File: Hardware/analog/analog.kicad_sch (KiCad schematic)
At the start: 0 parts

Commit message: Analog board tweaks
- Moved a few traces and components around to accomodate other changes
  in the controller stuff, preparation for some sort of cleanup

- Aesthetic moves of labels on controller board
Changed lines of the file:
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@@
     (stroke (width 0) (type default))
   )
-  (label "ISense_{0" (at 219.075 35.56 0) (fields_autoplaced)
+  (label "ISense_{0}" (at 219.075 35.56 0) (fields_autoplaced)
     (effects (font (size 1.27 1.27)) (justify left bottom))
   )
@@
     (effects (font (size 1.27 1.27)) (justify left bottom))
   )
-  (label "ISet_{0" (at 161.925 78.74 0) (fields_autoplaced)
-    (effects (font (size 1.27 1.27)) (justify left bottom))
-  )
-  (label "ISense_{1" (at 161.925 90.17 0) (fields_autoplaced)
-    (effects (font (size 1.27 1.27)) (justify left bottom))
-  )
-  (label "ISense_{1" (at 219.075 38.1 0) (fields_autoplaced)
+  (label "ISet_{0}" (at 161.925 78.74 0) (fields_autoplaced)
+    (effects (font (size 1.27 1.27)) (justify left bottom))
+  )
+  (label "ISense_{1}" (at 161.925 90.17 0) (fields_autoplaced)
+    (effects (font (size 1.27 1.27)) (justify left bottom))
+  )
+  (label "ISense_{1}" (at 219.075 38.1 0) (fields_autoplaced)
     (effects (font (size 1.27 1.27)) (justify left bottom))
   )
@@
     (effects (font (size 1.27 1.27)) (justify left bottom))
   )
-  (label "ISet_{1" (at 219.075 30.48 0) (fields_autoplaced)
-    (effects (font (size 1.27 1.27)) (justify left bottom))
-  )
-  (label "ISet_{1" (at 161.925 81.28 0) (fields_autoplaced)
+  (label "ISet_{1}" (at 219.075 30.48 0) (fields_autoplaced)
+    (effects (font (size 1.27 1.27)) (justify left bottom))
+  )
+  (label "ISet_{1}" (at 161.925 81.28 0) (fields_autoplaced)
     (effects (font (size 1.27 1.27)) (justify left bottom))
   )
@@
     (effects (font (size 1.27 1.27)) (justify left bottom))
   )
-  (label "ISet_{0" (at 219.075 27.94 0) (fields_autoplaced)
-    (effects (font (size 1.27 1.27)) (justify left bottom))
-  )
-  (label "ISense_{0" (at 161.925 85.09 0) (fields_autoplaced)
+  (label "ISet_{0}" (at 219.075 27.94 0) (fields_autoplaced)
+    (effects (font (size 1.27 1.27)) (justify left bottom))
+  )
+  (label "ISense_{0}" (at 161.925 85.09 0) (fields_autoplaced)
     (effects (font (size 1.27 1.27)) (justify left bottom))
   )
@@
     )
     (path "/ebb39e00-184a-4d9a-998d-a9c1346d5a30/8034a9d2-228a-47f5-9e42-60bb92940d1f"
-      (reference "R502") (unit 1) (value "10k") (footprint "Resistor_SMD:R_0805_2012Metric_Pad1.20x1.40mm_HandSolder")
+      (reference "R502") (unit 1) (value "5k6") (footprint "Resistor_SMD:R_0805_2012Metric_Pad1.20x1.40mm_HandSolder")
     )
     (path "/ebb39e00-184a-4d9a-998d-a9c1346d5a30/d4ade582-8aad-40e5-8e88-07c361125e22"

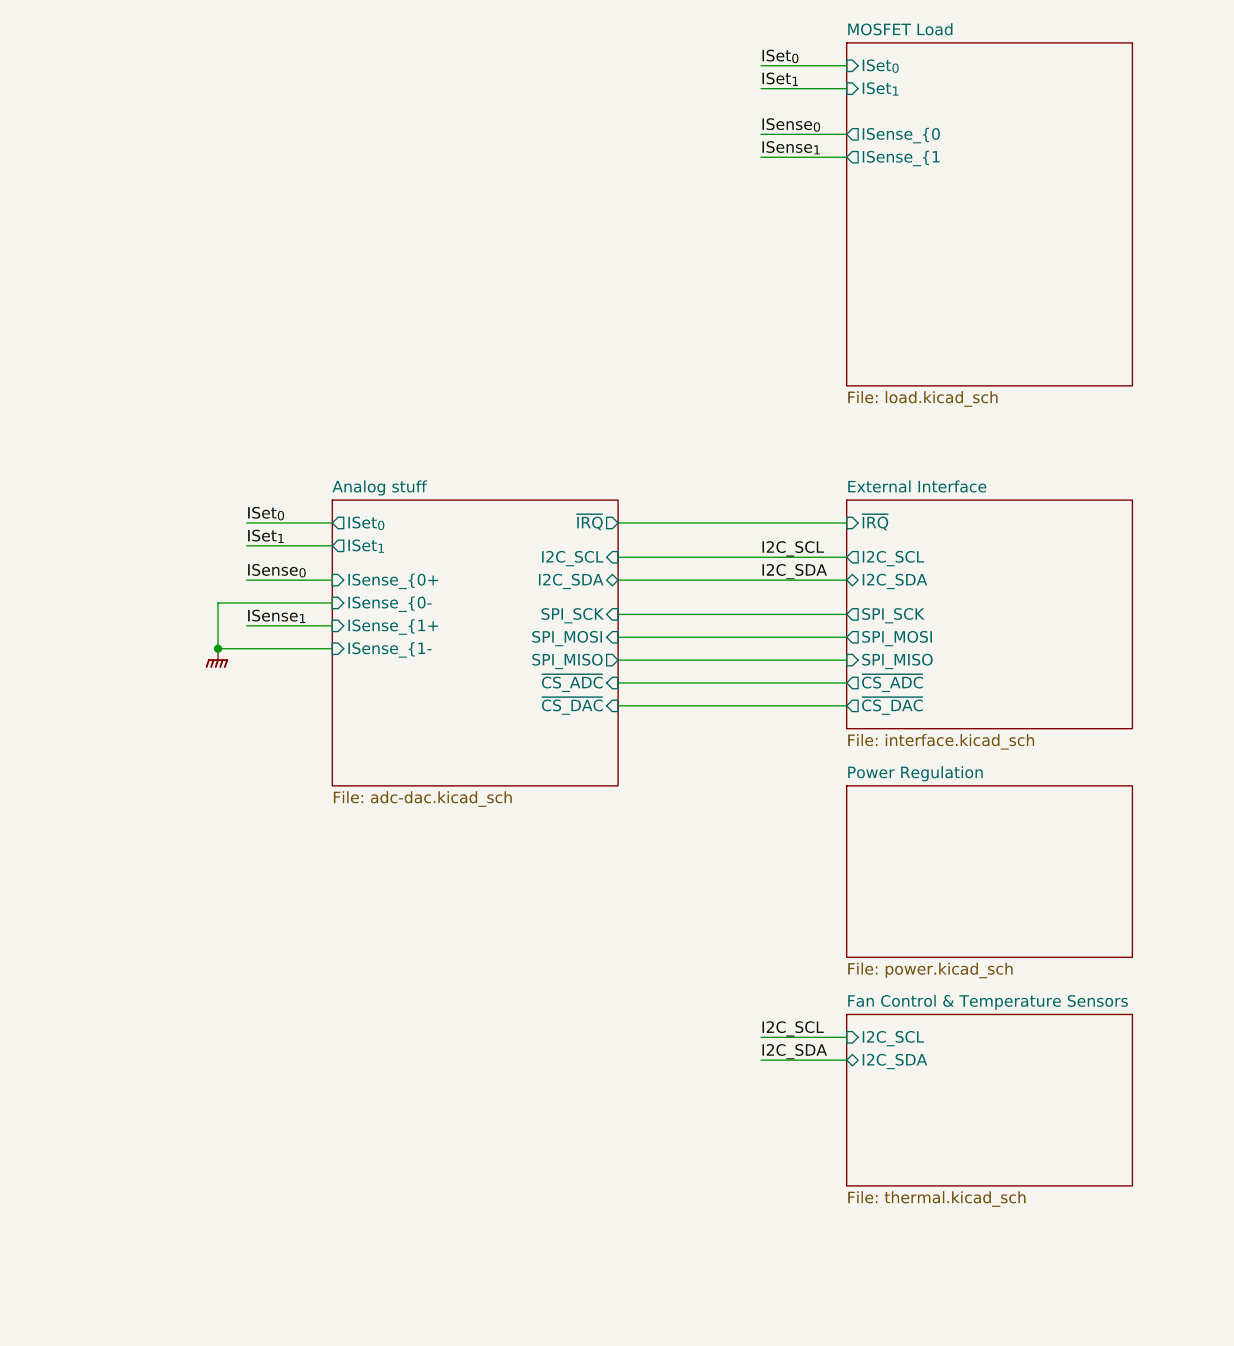
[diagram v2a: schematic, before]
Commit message: Analog board layout
- Started work on adding the voltage sense circuitry, including the
  selector relay, IO expander to drive the relay, and the second ADC to
  convert the voltage values

- Changed the layout of analog board to better take advantage of
  available space

- Minor changes to front panel layout for aesthetics
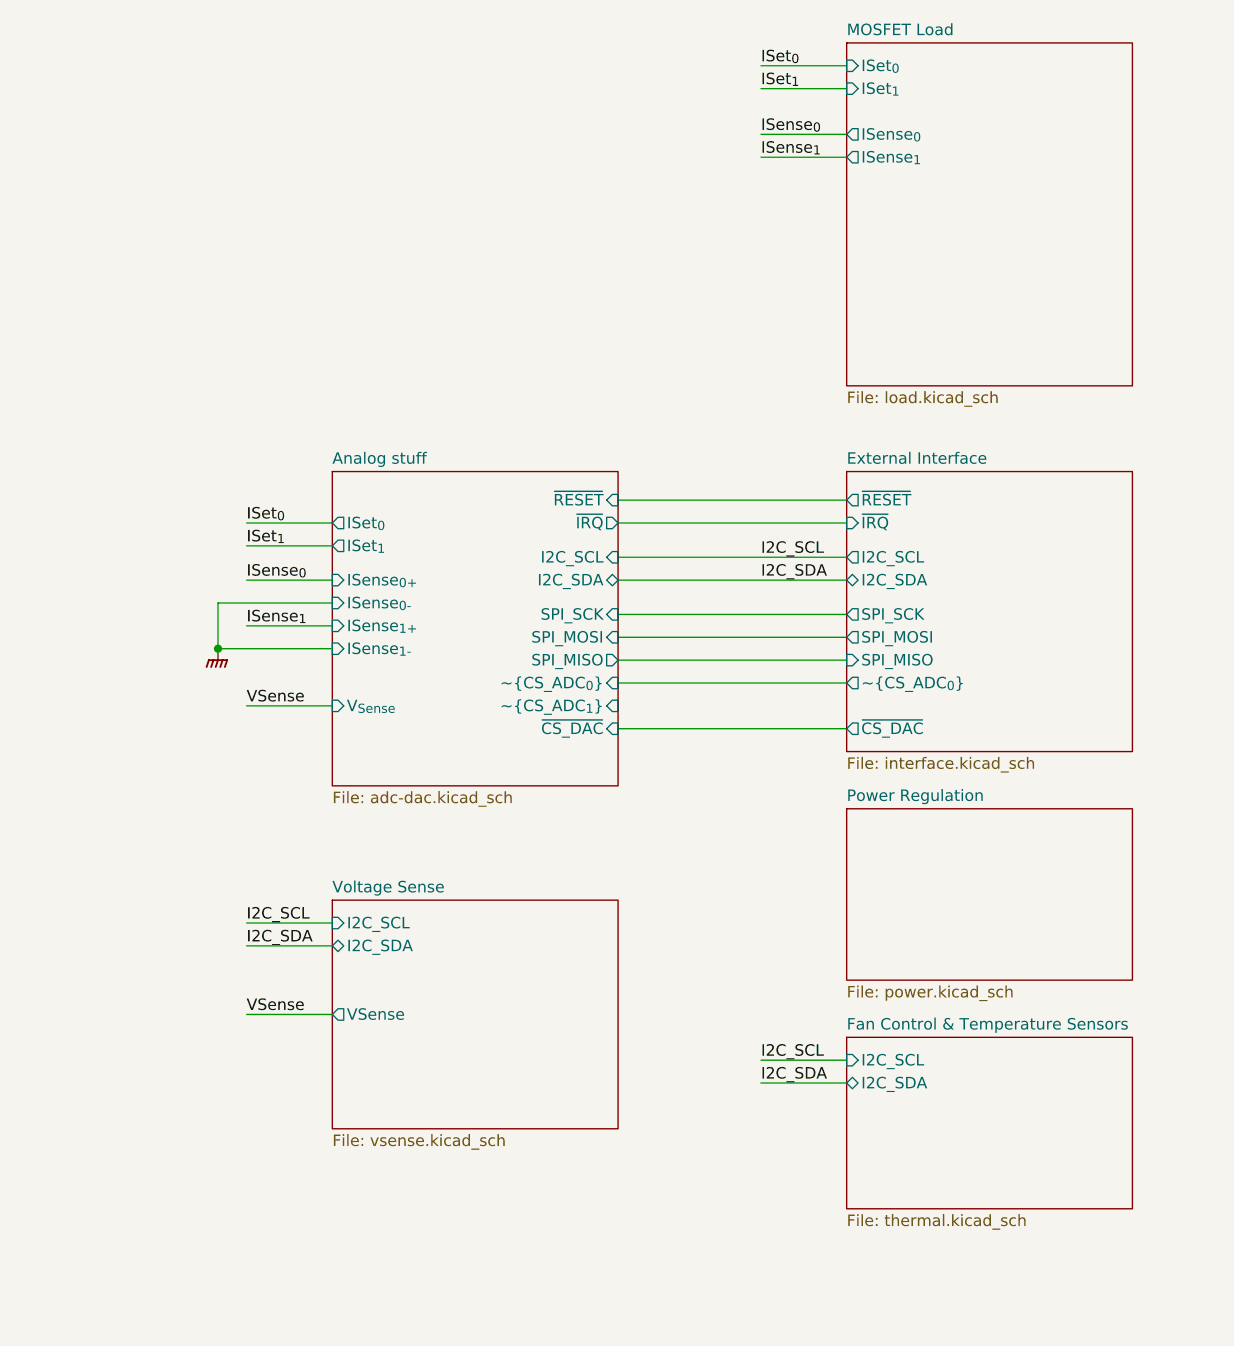
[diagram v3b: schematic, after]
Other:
- added sheet Voltage Sense (vsense.kicad_sch)
- sheet Analog stuff ports: added ISense_{0+}, ISense_{0-}, ISense_{1+}, ISense_{1-}, V_{Sense}, ~{CS_ADC_{0}}, ~{CS_ADC_{1}}, ~{RESET}; removed ISense_{0+, ISense_{0-, ISense_{1+, ISense_{1-, ~{CS_ADC}
- sheet External Interface ports: added ~{CS_ADC_{0}}, ~{RESET}; removed ~{CS_ADC}
- sheet MOSFET Load ports: added ISense_{0}, ISense_{1}; removed ISense_{0, ISense_{1

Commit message: Mostly finished up analog load board
- Finished routing most signals

- Connected relay drive to bonus I2C GPIO controller, and routed the
  rest of the voltage sense stuff

- Routed the reset signal to the DAC, so that when the board is reset,
  the current output will be reset to zero as well without processor
  intervention

- Replaced most passives with 0603/1608 size
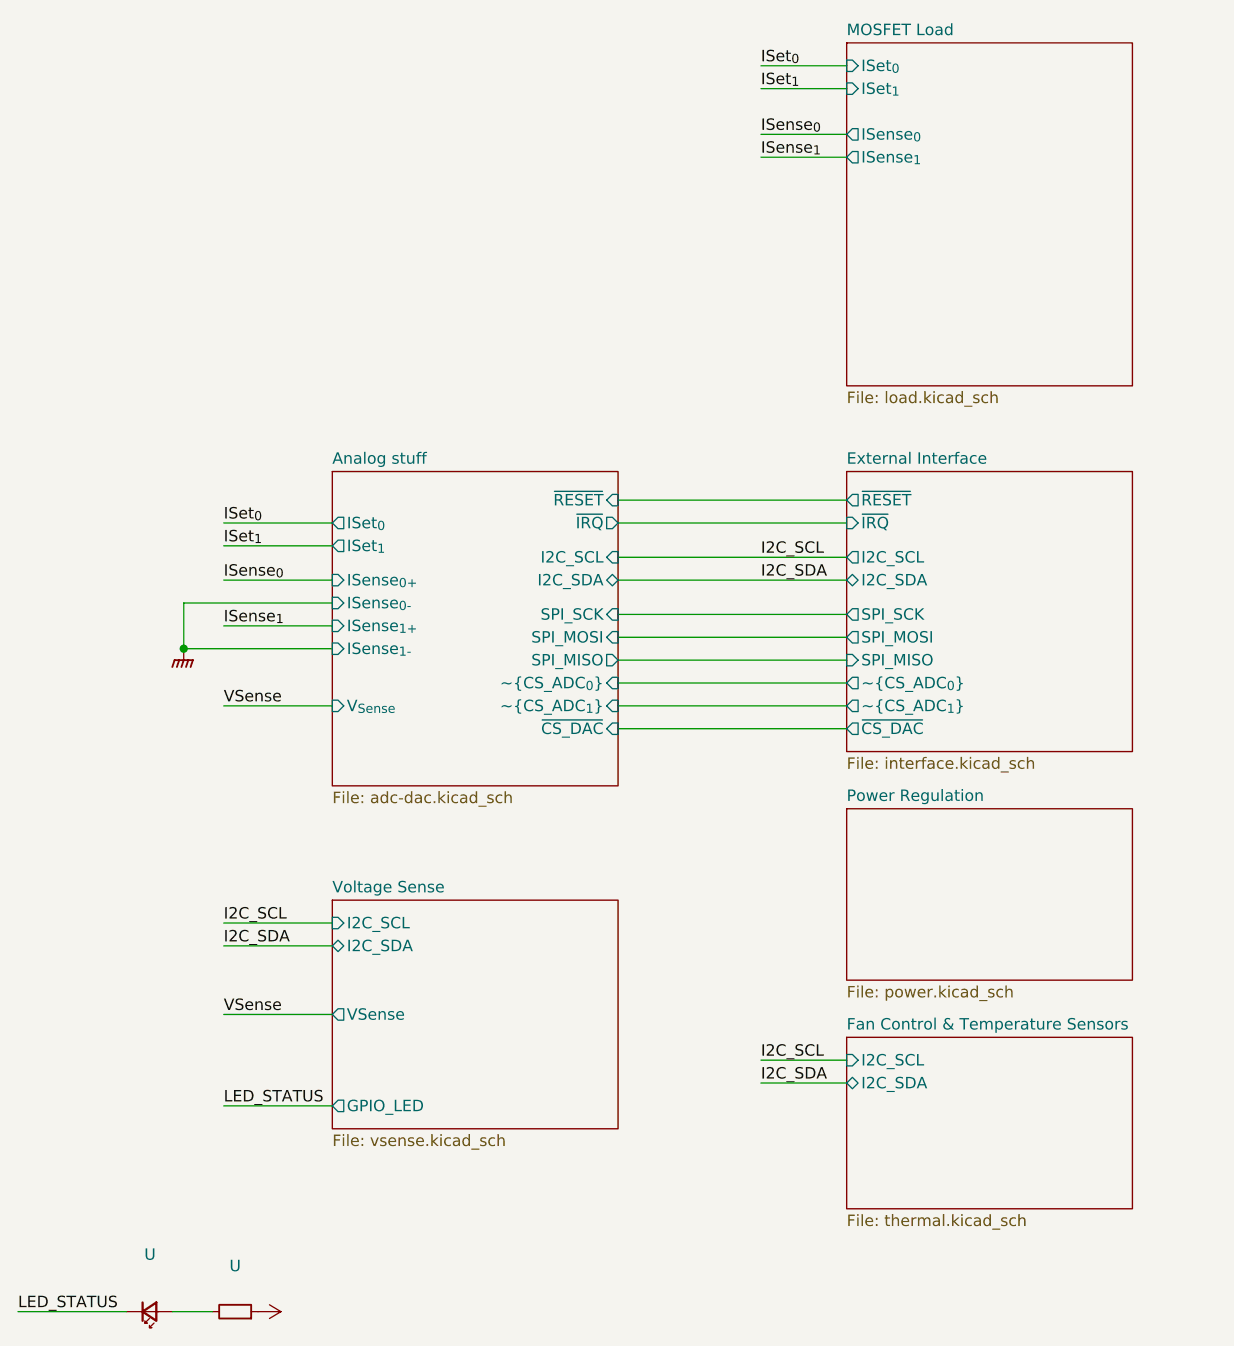
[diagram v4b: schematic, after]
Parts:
- added U: (no value), symbol Device:LED_Small
- added U: (no value), symbol Device:R_Small
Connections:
- new net: U.2, U.2 (A)
- new net +3V3: U.1
- new net LED_STATUS: U.1 (K)
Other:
- sheet External Interface ports: added ~{CS_ADC_{1}}; removed none
- sheet Voltage Sense ports: added GPIO_LED; removed none

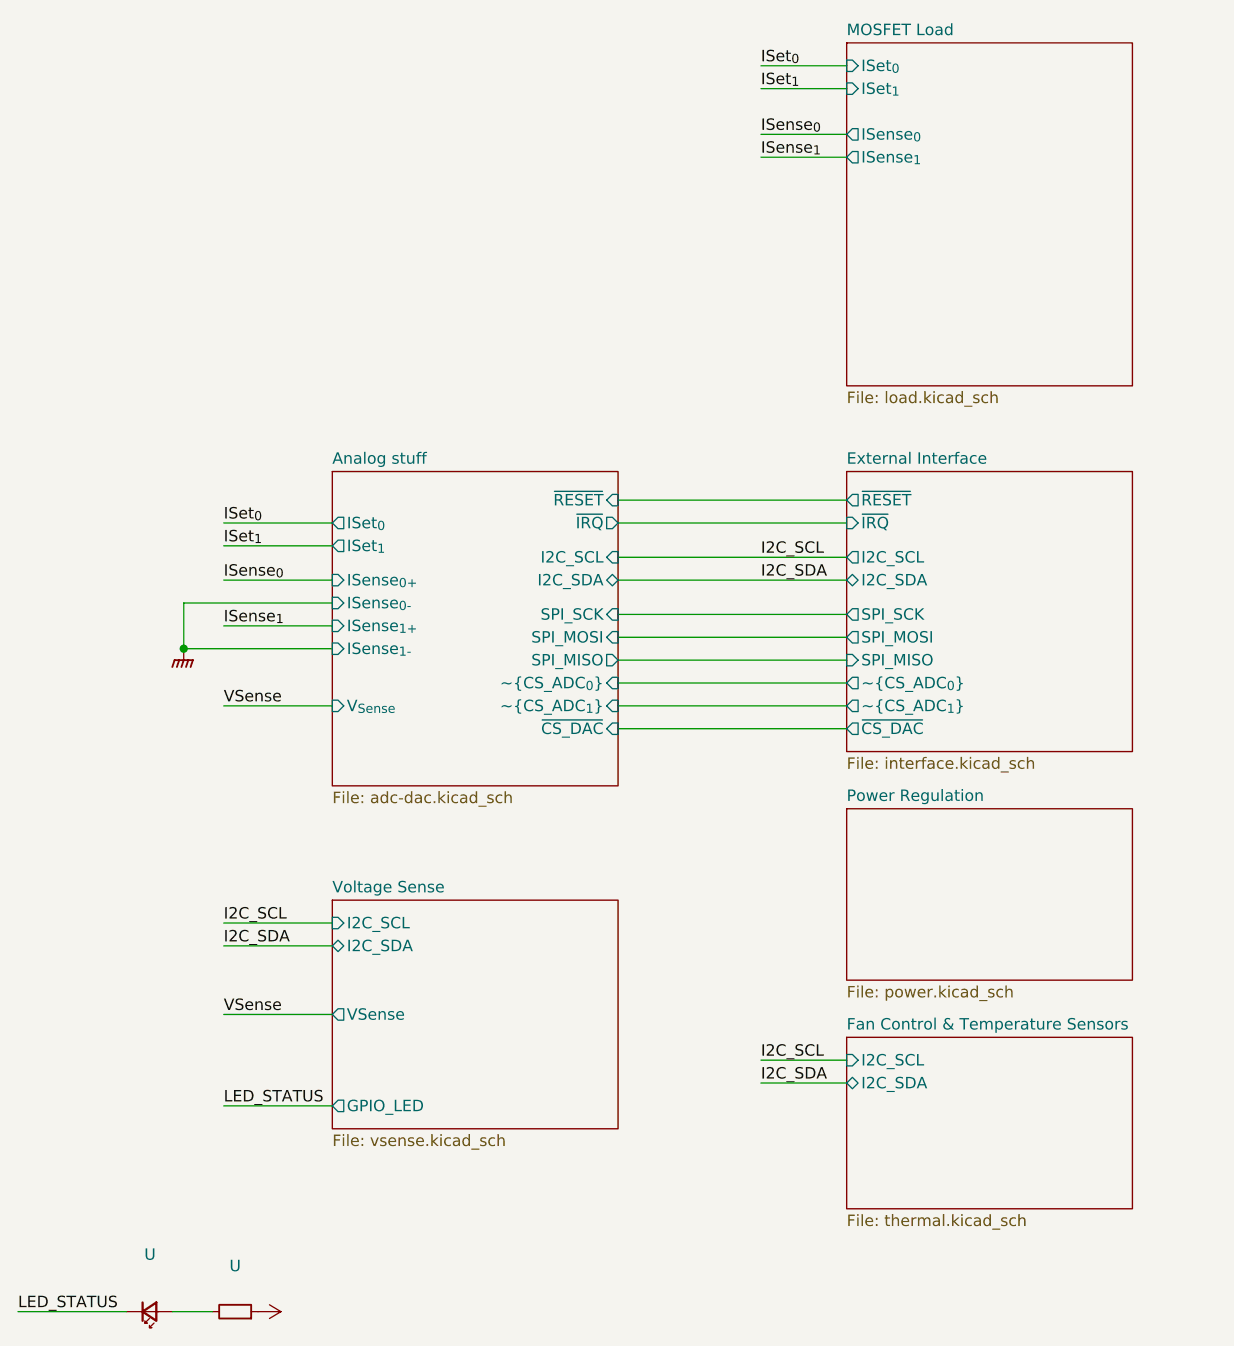
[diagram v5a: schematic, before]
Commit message: Temperature sensing & cleanup for analog board
- Added the auxiliary temperature sensing ADC, and routed it to the
  analog temperature sensors on the front and rear of the MOSFET
  heatsink

- Added an LM75 sensor to measure the analog board ambient temperature
  (for better temperature control/fan control)

  This may end up being a DNP item if it's not really useful or
  otherwise necessary.

- Fixes to a few symbols (namely pin directions) to pass ERC
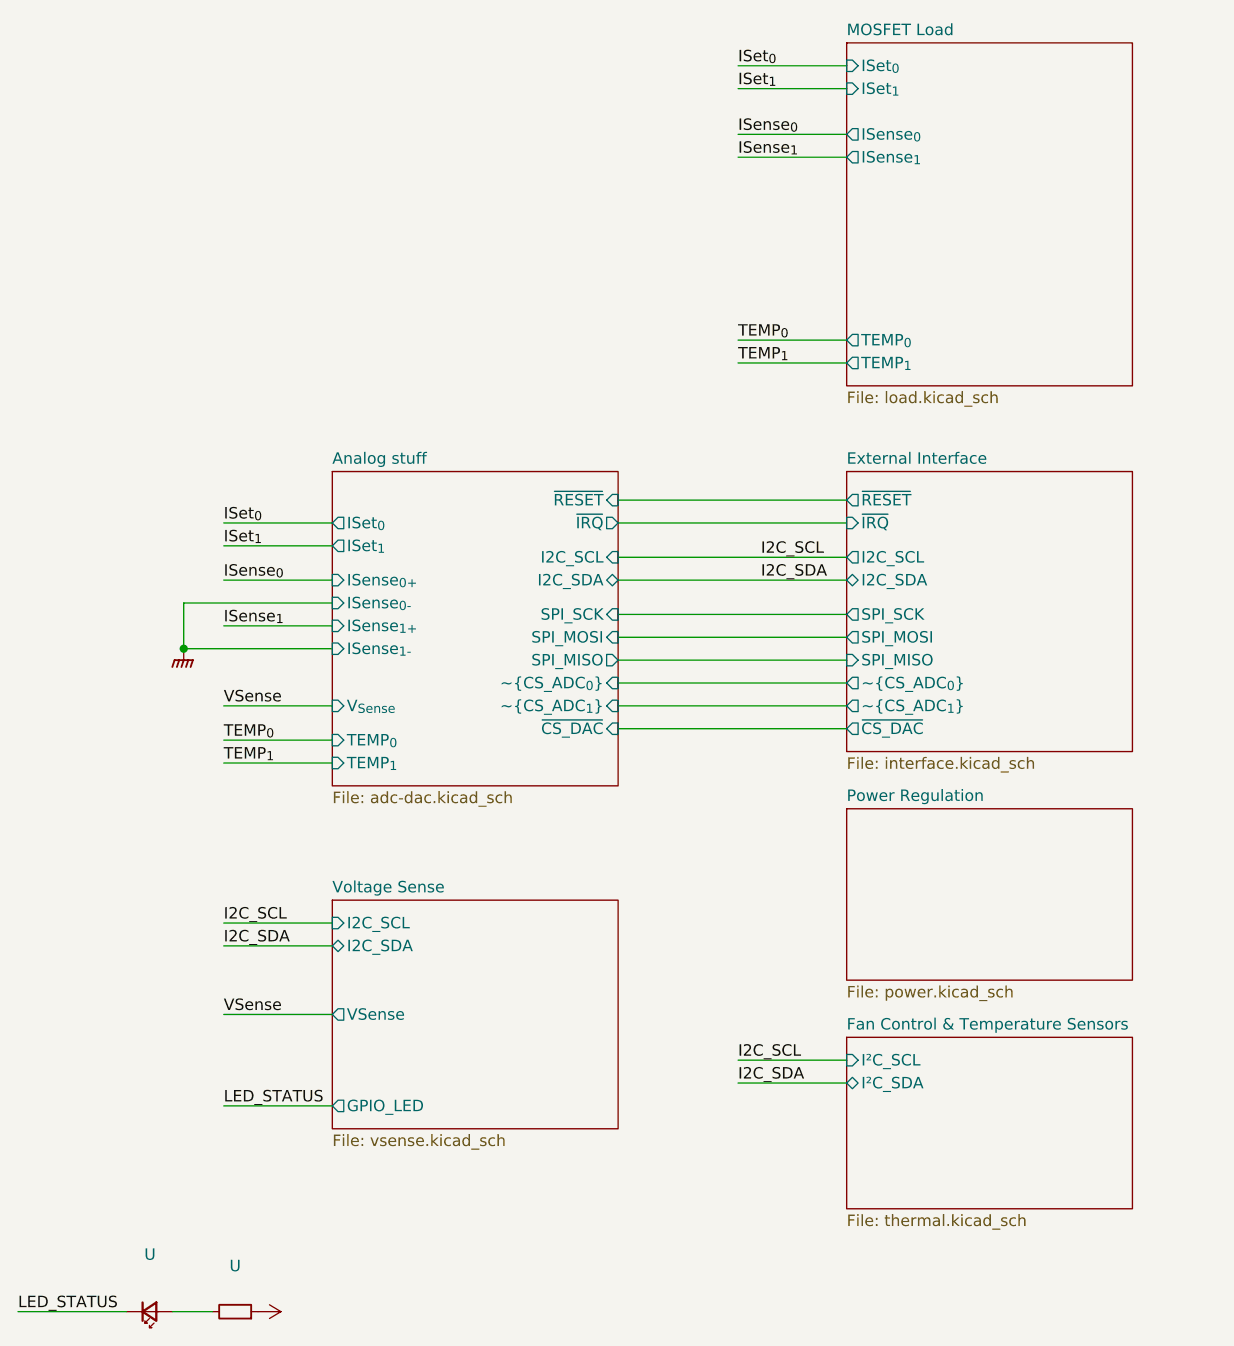
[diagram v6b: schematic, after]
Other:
- sheet Analog stuff ports: added TEMP_{0}, TEMP_{1}; removed none
- sheet Fan Control & Temperature Sensors ports: added I²C_SCL, I²C_SDA; removed I2C_SCL, I2C_SDA
- sheet MOSFET Load ports: added TEMP_{0}, TEMP_{1}; removed none
